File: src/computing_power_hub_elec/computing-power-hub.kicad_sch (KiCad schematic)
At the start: 49 parts, among them J109 SM02B-PASS, J110 IDC6, U101 STM32G474, U102 TCAN1462V, U103 ZD24C128A, Y101 24Mhz

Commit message: Grovel human! For this is ~~the Compute~~ Power ~~Module~~.
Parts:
- added H101, H102, H103: M2.5, Bluesat:M2.5, symbol Mechanical:MountingHole
- U101: value STM32G474 -> STM32G474_ComputePower; footprint Package_QFP:LQFP-64_10x10mm_P0.5mm -> Bluesat:LQFP-64-0.5
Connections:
- net ARGB_{0} is gone; now on net ARGB_{I,0}: U101.52 (PC10-ARGB_I)
- net IS_{24} is gone; now on net TEMP0: U101.21 (PA7-TMP_3)
- net VS_{12} is gone; now on net TEMP3: U101.12 (PA0-TMP_0)
- net VS_{24} is gone; now on net TEMP2: U101.13 (PA1-TMP_1)
- net VS_{BUS} is gone; now on net TEMP1: U101.17 (PA3-TMP_2)
- net ARGB_{I,0}: no longer U101.14 (PA2-ARGB_I)
- net I2C_SCL: now also U101.60 (PB7-I2C_SCL); no longer U101.51 (PA15-I2C_SCL)
- net I2C_SDA: now also U101.51 (PA15-I2C_SDA); no longer U101.60 (PB7-I2C_SDA)
- net TEMP0: no longer U101.36 (PB14-TMP_0)
- net TEMP1: no longer U101.8 (PC0-TMP_1)
- net TEMP2: no longer U101.9 (PC1-TMP_2)
- net TEMP3: no longer U101.22 (PC4-TMP_3)
- net Regulators/VS_{5V}: now reaches U101.10 (PC2-VS_5)
- net ARGB_{1} renamed Connectors/ARGB_{0}
- net ARGB_{2}: no longer names the net of U101.59 (PB6)
- net ARGB_{3} renamed Connectors/ARGB_{2}
- net EN_{12} renamed Connectors/NEN_{5VA}
- net EN_{19} renamed Regulators/EN_{19V}
- net EN_{24} renamed Regulators/EN_{24V}
- net EN_{5} renamed Connectors/NEN_{5VB}
- net IS_{12,M} renamed IS_{5A,M}
- net IS_{12,O} renamed IS_{5A,O}
- net IS_{12} renamed Connectors/IS_{5VA}
- net IS_{19} renamed Connectors/IS_{24V}
- net IS_{5,M} renamed IS_{5B,M}
- net IS_{5B,M}: now also U101.42 (PA8-IS_5B_O); no longer U101.37 (PB15-IS_5_M)
- net IS_{5,O} renamed IS_{5B,O}
- net IS_{5B,O}: now also U101.37 (PB15-IS_5B_M); no longer U101.42 (PA8-IS_5_O)
- net IS_{5} renamed Connectors/IS_{5VB}
- net VS_{19} renamed Connectors/IS_{19V}
- net VS_{5}: no longer names the net of U101.43 (PA9)
- new net Connectors/ARGB_{1}: U101.14 (PA2-ARGB_1)
- new net Connectors/ARGB_{3}: U101.22 (PC4-ARGB_3)
- new net Connectors/VS_{VBUS}: U101.36 (PB14-VS_BUS)
- new net Regulators/VS_{19V}: U101.9 (PC1-VS_19)
- new net Regulators/VS_{24V}: U101.8 (PC0-VS_24)
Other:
- sheet Connectors ports: added IS_{5VA}, IS_{5VB}, NEN_{5VA}, NEN_{5VB}; removed IS_{12V}, IS_{5V}, NEN_{12V}, NEN_{5V}
- sheet Regulators ports: added none; removed VS_{12V}
- moved on the sheet: C106, C107, C108, C109, C110, C111, C112, C114, C115, C116, C117, D101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

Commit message: Fix header again
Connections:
- net DBG.NRST: now also J110.5 (Pin_5); no longer J110.2 (Pin_2)
- net DBG.SWCLK: now also J110.1 (Pin_1); no longer J110.6 (Pin_6)
- net DBG.SWDIO: now also J110.2 (Pin_2); no longer J110.5 (Pin_5)
- net DBG.SWO: now also J110.6 (Pin_6); no longer J110.1 (Pin_1)
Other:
- moved on the sheet: J110
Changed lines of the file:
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@@
 	(wire
 		(pts
+			(xy 78.74 104.14) (xy 85.09 104.14)
+		)
+		(stroke
+			(width 0)
+			(type default)
+		)
+	)
+	(wire
+		(pts
 			(xy 125.73 81.28) (xy 128.27 81.28)
 		)
@@
 	(wire
 		(pts
+			(xy 78.74 99.06) (xy 85.09 99.06)
+		)
+		(stroke
+			(width 0)
+			(type default)
+		)
+	)
+	(wire
+		(pts
 			(xy 106.68 27.94) (xy 132.08 27.94)
 		)
@@
 	(wire
 		(pts
-			(xy 85.09 104.14) (xy 78.74 104.14)
-		)
-		(stroke
-			(width 0)
-			(type default)
-		)
-	)
-	(wire
-		(pts
 			(xy 125.73 71.12) (xy 128.27 71.12)
 		)
@@
 	(wire
 		(pts
-			(xy 85.09 99.06) (xy 78.74 99.06)
-		)
-		(stroke
-			(width 0)
-			(type default)
-		)
-	)
-	(wire
-		(pts
 			(xy 194.31 149.86) (xy 194.31 147.32)
 		)
@@
 	(symbol
 		(lib_id "power:GND")
-		(at 97.79 101.6 90)
-		(mirror x)
+		(at 85.09 101.6 270)
 		(unit 1)
 		(exclude_from_sim no)
@@
 		(dnp no)
 		(property "Reference" "#PWR0194"
-			(at 104.14 101.6 0)
+			(at 78.74 101.6 0)
 			(effects
 				(font
@@
 		)
 		(property "Value" "GND"
-			(at 100.33 101.6 90)
+			(at 82.55 101.6 90)
 			(effects
 				(font
@@
 		)
 		(property "Footprint" ""
-			(at 97.79 101.6 0)
+			(at 85.09 101.6 0)
 			(effects
 				(font
@@
 		)
 		(property "Datasheet" ""
-			(at 97.79 101.6 0)
+			(at 85.09 101.6 0)
 			(effects
 				(font
@@
 		)
 		(property "Description" "Power symbol creates a global label with name \"GND\" , ground"
-			(at 97.79 101.6 0)
+			(at 85.09 101.6 0)
 			(effects
 				(font
@@
 	(symbol
 		(lib_id "Connector_Generic:Conn_02x03_Odd_Even")
-		(at 90.17 101.6 0)
+		(at 92.71 101.6 180)
 		(unit 1)
 		(exclude_from_sim no)
@@
 		(dnp no)
 		(property "Reference" "J110"
-			(at 91.44 93.98 0)
+			(at 91.44 109.22 0)
 			(effects
 				(font
@@
 		)
 		(property "Value" "IDC6"
-			(at 91.44 96.52 0)
+			(at 91.44 106.68 0)
 			(effects
 				(font
@@
 		)
 		(property "Footprint" "Bluesat:IDC6"
-			(at 90.17 101.6 0)
+			(at 92.71 101.6 0)
 			(effects
 				(font
@@
 		)
 		(property "Datasheet" "~"
-			(at 90.17 101.6 0)
+			(at 92.71 101.6 0)
 			(effects
 				(font
@@
 		)
 		(property "Description" "Generic connector, double row, 02x03, odd/even pin numbering scheme (row 1 odd numbers, row 2 even numbers), script generated (kicad-library-utils/schlib/autogen/connector/)"
-			(at 90.17 101.6 0)
+			(at 92.71 101.6 0)
 			(effects
 				(font
@@
 	(symbol
 		(lib_id "power:VDD")
-		(at 85.09 101.6 90)
+		(at 97.79 101.6 270)
+		(mirror x)
 		(unit 1)
 		(exclude_from_sim no)
@@
 		(dnp no)
 		(property "Reference" "#PWR0193"
-			(at 88.9 101.6 0)
+			(at 93.98 101.6 0)
 			(effects
 				(font
@@
 		)
 		(property "Value" "VDD"
-			(at 82.55 101.6 90)
+			(at 100.33 101.6 90)
 			(effects
 				(font
@@
 		)
 		(property "Footprint" ""
-			(at 85.09 101.6 0)
+			(at 97.79 101.6 0)
 			(effects
 				(font
@@
 		)
 		(property "Datasheet" ""
-			(at 85.09 101.6 0)
+			(at 97.79 101.6 0)
 			(effects
 				(font
@@
 		)
 		(property "Description" "Power symbol creates a global label with name \"VDD\""
-			(at 85.09 101.6 0)
+			(at 97.79 101.6 0)
 			(effects
 				(font

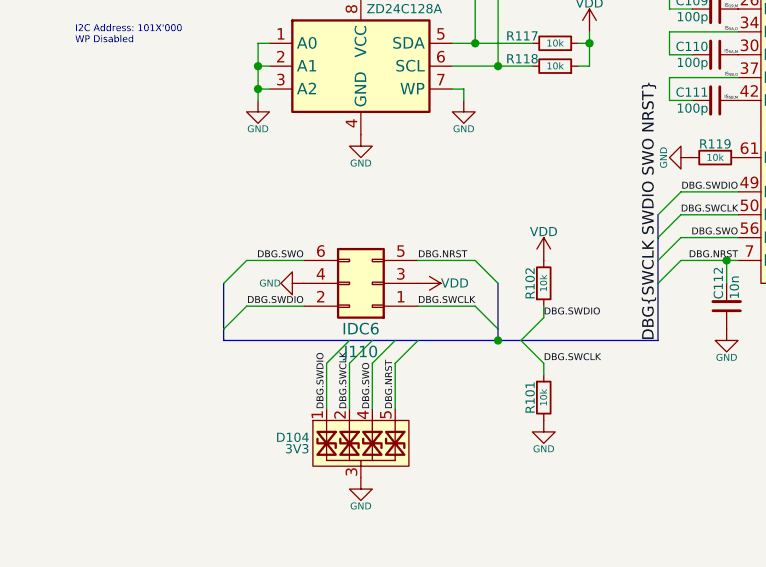
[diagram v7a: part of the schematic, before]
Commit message: Fix rotated IDC6 on CPM/MPM/VESC/Stepper/USB Hub (#120)
* Fix rotated IDC6 on CPM/MPM/VESC/Stepper/USB Hub

* Fix VESC
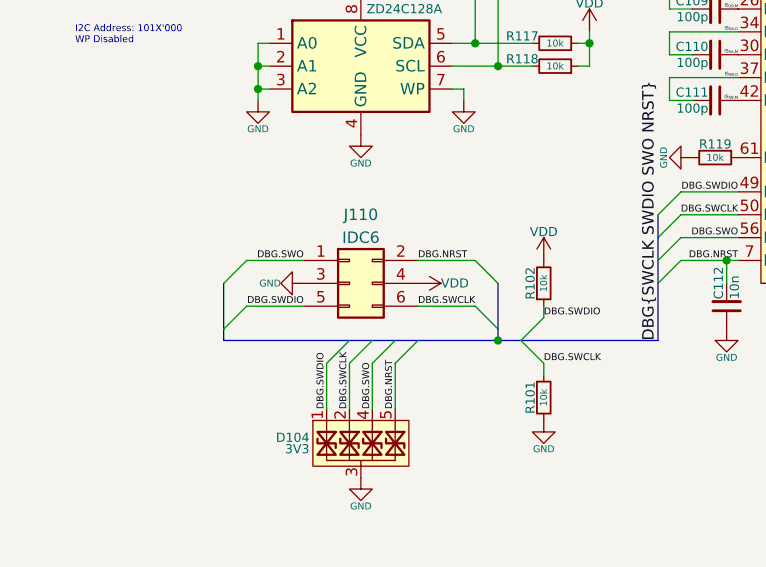
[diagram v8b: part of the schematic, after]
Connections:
- net DBG.NRST: now also J110.2 (Pin_2); no longer J110.5 (Pin_5)
- net DBG.SWCLK: now also J110.6 (Pin_6); no longer J110.1 (Pin_1)
- net DBG.SWDIO: now also J110.5 (Pin_5); no longer J110.2 (Pin_2)
- net DBG.SWO: now also J110.1 (Pin_1); no longer J110.6 (Pin_6)
- net GND: now also J110.3 (Pin_3); no longer J110.4 (Pin_4)
- net VDD: now also J110.4 (Pin_4); no longer J110.3 (Pin_3)
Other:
- moved on the sheet: J110
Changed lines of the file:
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@@
 	(symbol
 		(lib_id "Connector_Generic:Conn_02x03_Odd_Even")
-		(at 92.71 101.6 180)
+		(at 90.17 101.6 0)
 		(unit 1)
 		(exclude_from_sim no)
@@
 		(dnp no)
 		(property "Reference" "J110"
-			(at 91.44 109.22 0)
+			(at 91.44 93.98 0)
 			(effects
 				(font
@@
 		)
 		(property "Value" "IDC6"
-			(at 91.44 106.68 0)
+			(at 91.44 96.52 0)
 			(effects
 				(font
@@
 		)
 		(property "Footprint" "Bluesat:IDC6"
-			(at 92.71 101.6 0)
+			(at 90.17 101.6 0)
 			(effects
 				(font
@@
 		)
 		(property "Datasheet" "~"
-			(at 92.71 101.6 0)
+			(at 90.17 101.6 0)
 			(effects
 				(font
@@
 		)
 		(property "Description" "Generic connector, double row, 02x03, odd/even pin numbering scheme (row 1 odd numbers, row 2 even numbers), script generated (kicad-library-utils/schlib/autogen/connector/)"
-			(at 92.71 101.6 0)
+			(at 90.17 101.6 0)
 			(effects
 				(font
